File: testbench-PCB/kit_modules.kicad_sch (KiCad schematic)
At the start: 22 parts, among them U2 Rotary_encoder_switch_module, U3 Thermistor_module, U4 Relay_module, U6 Matrix_keyboard, U7 RTC_EEPROM_module, U8 LCD_display

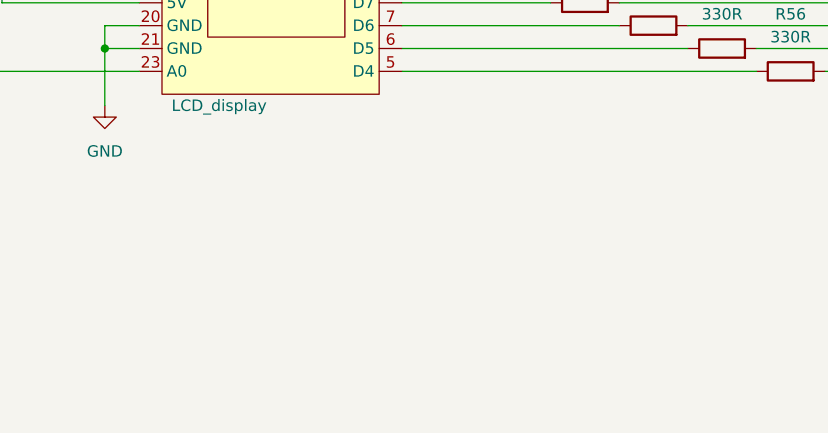
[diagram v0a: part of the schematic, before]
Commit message: Added titles to schematics.
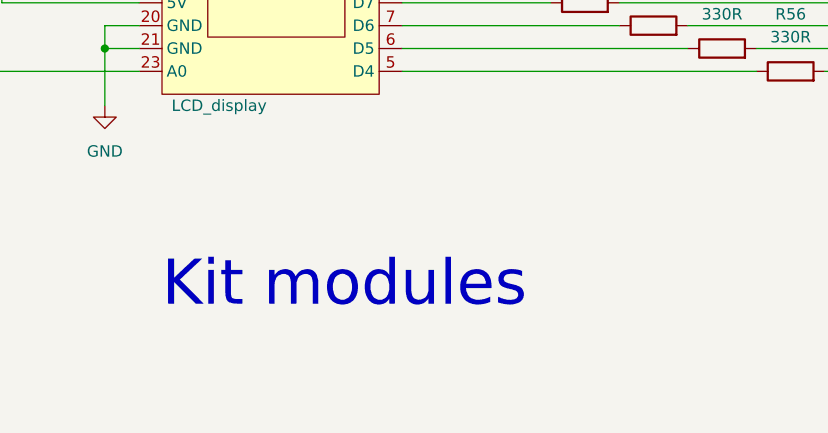
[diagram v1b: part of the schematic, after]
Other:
- note added: "Kit modules"
- company: (none) -> Company: VUT Brno
- title: (none) -> Test benches for microcontroller kits
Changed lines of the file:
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@@
 (kicad_sch (version 20230121) (generator eeschema)
   (paper "A4")
+  (title_block
+    (title "Test benches for microcontroller kits")
+    (date "2023")
+    (rev "v0.1")
+    (company "Company: VUT Brno")
+    (comment 1 "Author: Ivo Zaludek")
+  )
   (bus_alias "I2C" (members "I2C_SDA" "I2C_SCL"))
   (bus_alias "RELAY_IO" (members "K1-IN" "K2-IN" "K1-NC" "K1-NO" "K2-NC" "K2-NO"))
@@
     (stroke (width 0) (type default))
   )
+  (text "Kit modules" (at 177.8 173.99 0)
+    (effects (font (size 5 5)) (justify left bottom))
+  )
   (label "K2-NC" (at 251.46 52.07 180) (fields_autoplaced)
